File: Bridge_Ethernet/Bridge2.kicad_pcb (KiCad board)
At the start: 2 copper layers, 62 x 82 mm, 82 parts, among them J1 Conn_01x04_Female, J2 Conn_01x04_Female, J3 Conn_01x06, J4 Conn_01x06, J5 Conn_2Rows-13Pins, J7 Conn_01x04_Male, U1 MAX3222CDW, U10 MAX3222CDW, U11 ISL83485, U12 MAX3222CDW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

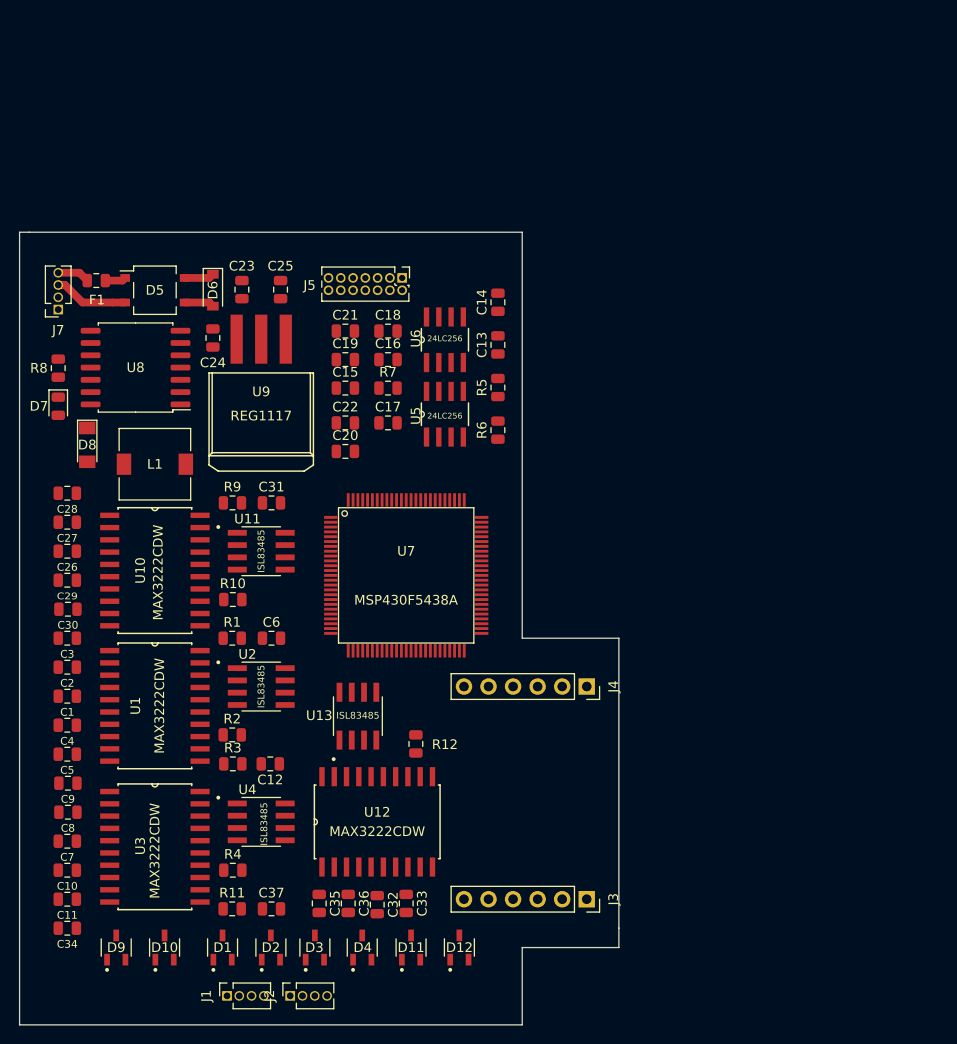
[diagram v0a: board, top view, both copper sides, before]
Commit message: Esquemático Finalizado. Asignaciones Realizadas. Reacomodamiento de componentes. Inicio de Ruteo.
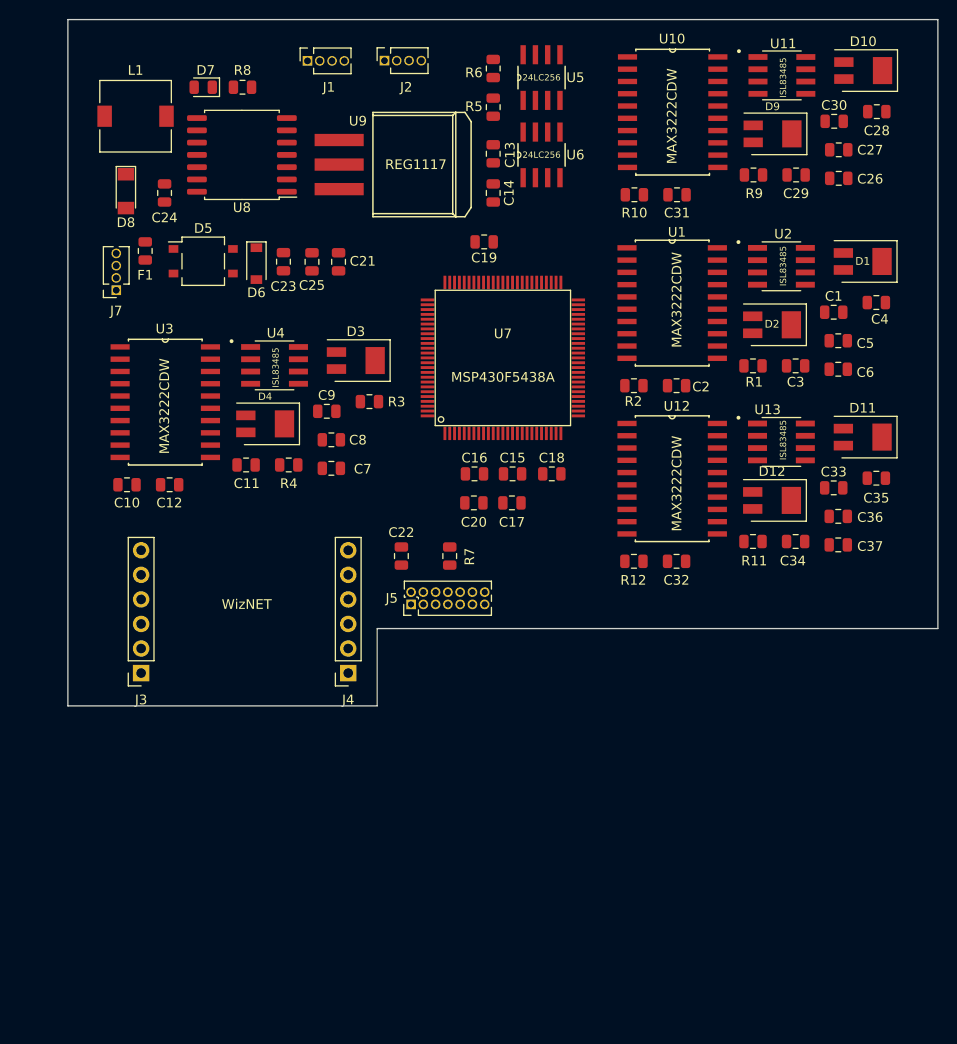
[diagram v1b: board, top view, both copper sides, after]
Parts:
- D1, D10, D11, D12, D2, D3, D4, D9: footprint SOT95P280X125-3N:SOT95P280X125-3N -> Diode_SMD:D_SMB_Modified
- moved D10 116.0 mm to (108.3, 56.3), turned to 0 degrees
- moved D9 108.1 mm to (98.9, 62.8), turned to 0 degrees
- moved J2 97.2 mm to (58.8, 55.2)
- moved J1 97.1 mm to (50.8, 55.3)
- moved D1 97.1 mm to (108.2, 76.0), turned to 0 degrees
- moved C4 94.4 mm to (109.6, 80.3), turned to 0 degrees
- moved C30 94.0 mm to (105.3, 61.5), turned to 0 degrees
- moved C28 92.6 mm to (109.7, 60.5), turned to 0 degrees
- moved C5 90.5 mm to (105.7, 84.2), turned to 0 degrees
- moved C1 88.7 mm to (105.2, 81.3), turned to 0 degrees
- moved C26 88.6 mm to (105.7, 67.4), turned to 0 degrees
- moved C27 88.6 mm to (105.7, 64.5), turned to 0 degrees
- moved C29 86.3 mm to (101.3, 67.1), turned to 0 degrees
- moved C34 85.3 mm to (101.3, 105.0), turned to 0 degrees
- moved D2 82.7 mm to (98.8, 82.6), turned to 0 degrees
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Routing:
- net /Alimentación/VCC2: track 7.67 -> 0.00 mm
- net /Alimentación/VCC1: track 3.34 -> 0.00 mm
- net VCC: track 3.08 -> 0.00 mm
- net GND: track 3.08 -> 0.00 mm
- net Net-(D5-Pad1): track 2.16 -> 0.00 mm
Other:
- board size 62 x 82 mm -> 90 x 71 mm
- board text added: "Alimentación"
- board text added: "Drivers Serie 0, 1 y 2"
- board text added: "Drivers Serie 3"
- board text added: "Memorias"
- board text added: "Micro"
- board text added: "WizNET"
